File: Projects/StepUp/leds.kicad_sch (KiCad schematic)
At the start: 1 part

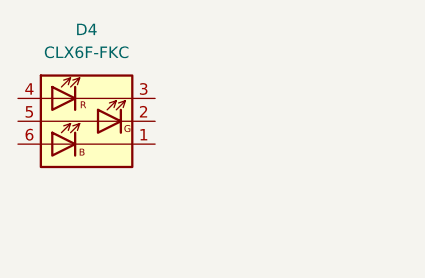
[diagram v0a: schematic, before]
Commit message: feat(stepup): Schematic + PCB updates
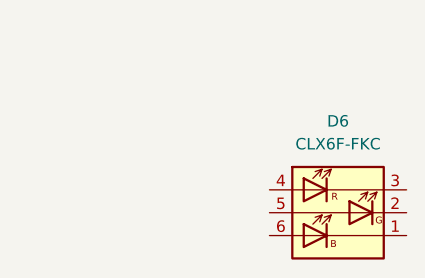
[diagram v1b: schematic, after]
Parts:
- renumbered D4 to D6
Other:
- moved on the sheet: D6
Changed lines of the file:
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@@
 	(symbol
 		(lib_id "LED:CLX6F-FKC")
-		(at 180.34 137.16 0)
+		(at 208.28 147.32 0)
 		(unit 1)
 		(exclude_from_sim no)
@@
 		(dnp no)
 		(fields_autoplaced yes)
-		(property "Reference" "D4"
-			(at 180.34 127 0)
+		(property "Reference" "D6"
+			(at 208.28 137.16 0)
 			(effects
 				(font
@@
 		)
 		(property "Value" "CLX6F-FKC"
-			(at 180.34 129.54 0)
+			(at 208.28 139.7 0)
 			(effects
 				(font
@@
 		)
 		(property "Footprint" "LED_SMD:LED_RGB_PLCC-6"
-			(at 175.26 145.288 0)
+			(at 203.2 155.448 0)
 			(effects
 				(font
@@
 		)
 		(property "Datasheet" "https://assets.cree-led.com/a/ds/h/HB-CLX6F-FKC.pdf"
-			(at 184.15 137.16 0)
+			(at 212.09 147.32 0)
 			(effects
 				(font
@@
 		)
 		(property "Description" "RGB LED, PLCC-6 "
-			(at 180.34 137.16 0)
+			(at 208.28 147.32 0)
 			(effects
 				(font
@@
 			(project "StepUp"
 				(path "/e0cca1c7-c263-49eb-8c40-74000ebe5285/b287fd2a-b2a9-45b4-81d1-0975d80d8cfc"
-					(reference "D4")
+					(reference "D6")
 					(unit 1)
 				)

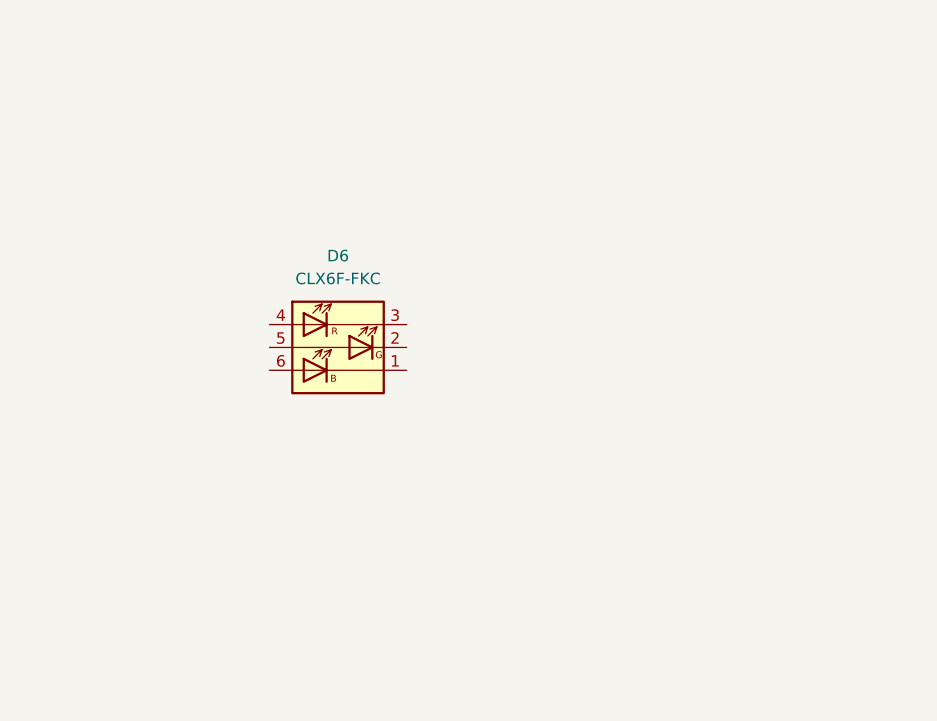
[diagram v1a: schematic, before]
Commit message: feat(schematic): Ready for layout
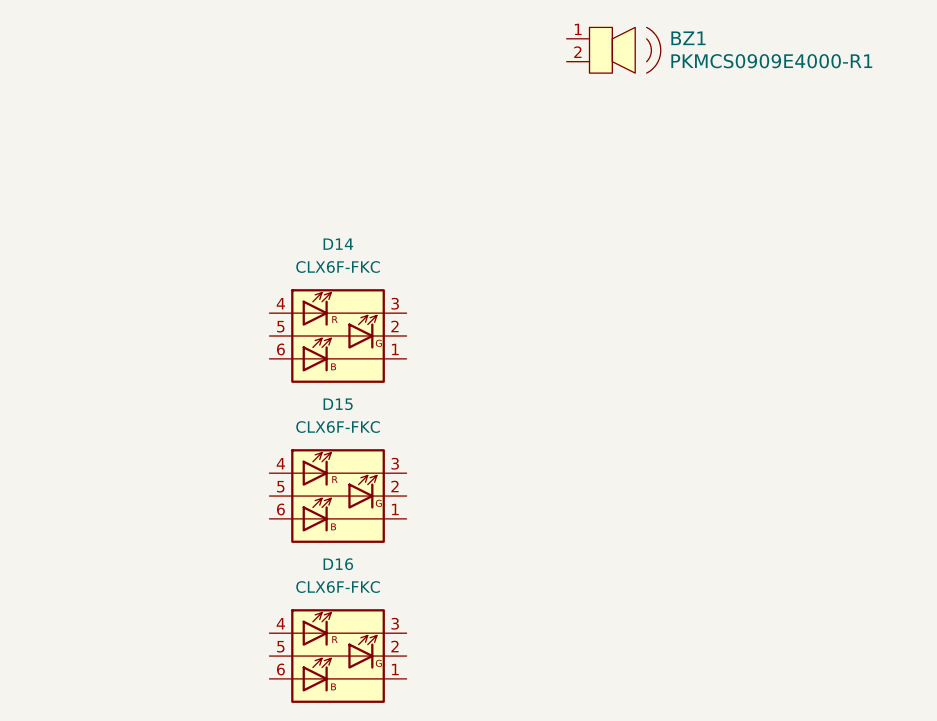
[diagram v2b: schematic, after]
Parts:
- added BZ1: PKMCS0909E4000-R1, digikey-footprints:Piezo_9x9mm_PKMCS0909E4000-R1, symbol dk_Alarms-Buzzers-and-Sirens:PKMCS0909E4000-R1
- added D15, D16: CLX6F-FKC, LED_SMD:LED_RGB_PLCC-6, symbol LED:CLX6F-FKC
- renumbered D6 to D14
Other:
- moved on the sheet: D14
